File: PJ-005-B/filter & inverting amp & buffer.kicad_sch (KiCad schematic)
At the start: 27 parts, among them U11 AD8608ARUZ-REEL, U12 AD8608ARUZ-REEL

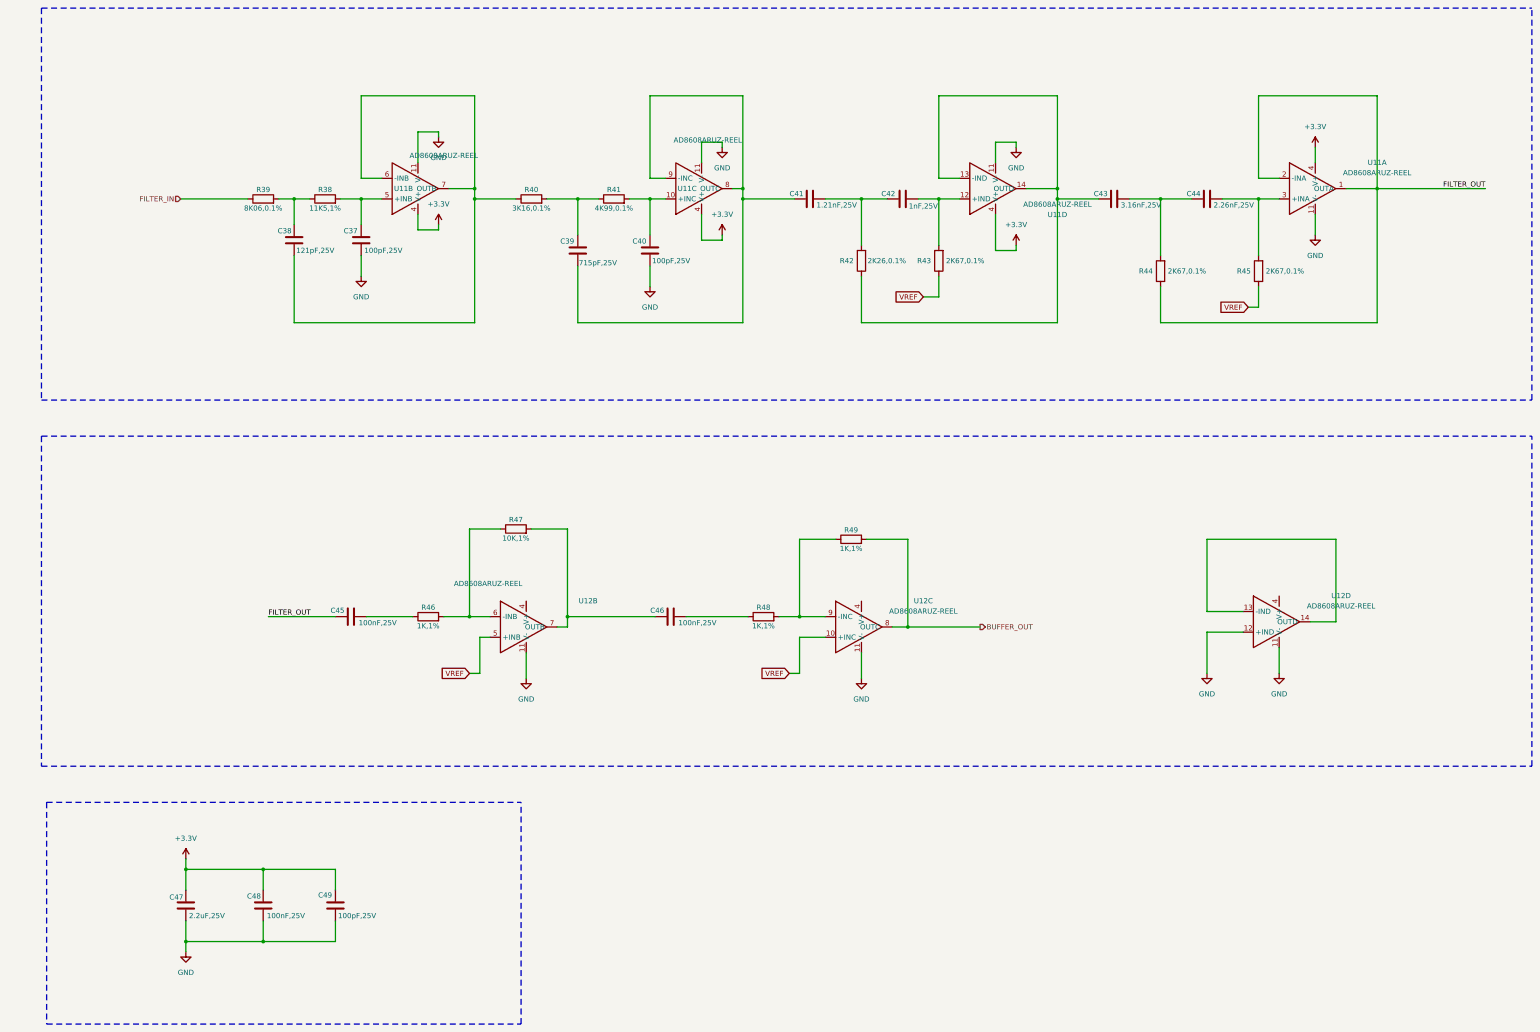
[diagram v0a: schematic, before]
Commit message: -- Receive stage with charge amp-->inverting amp-->BPF-->inverting amp-->buffer-->PGA-->buffer -- Transmit stage with push pull mosfet -- TTL to RS485 converter -- LDOs 12V to 9V, 9V to 6V, 6V to 5V, 5V to 2.5V and -5V to -2.5V
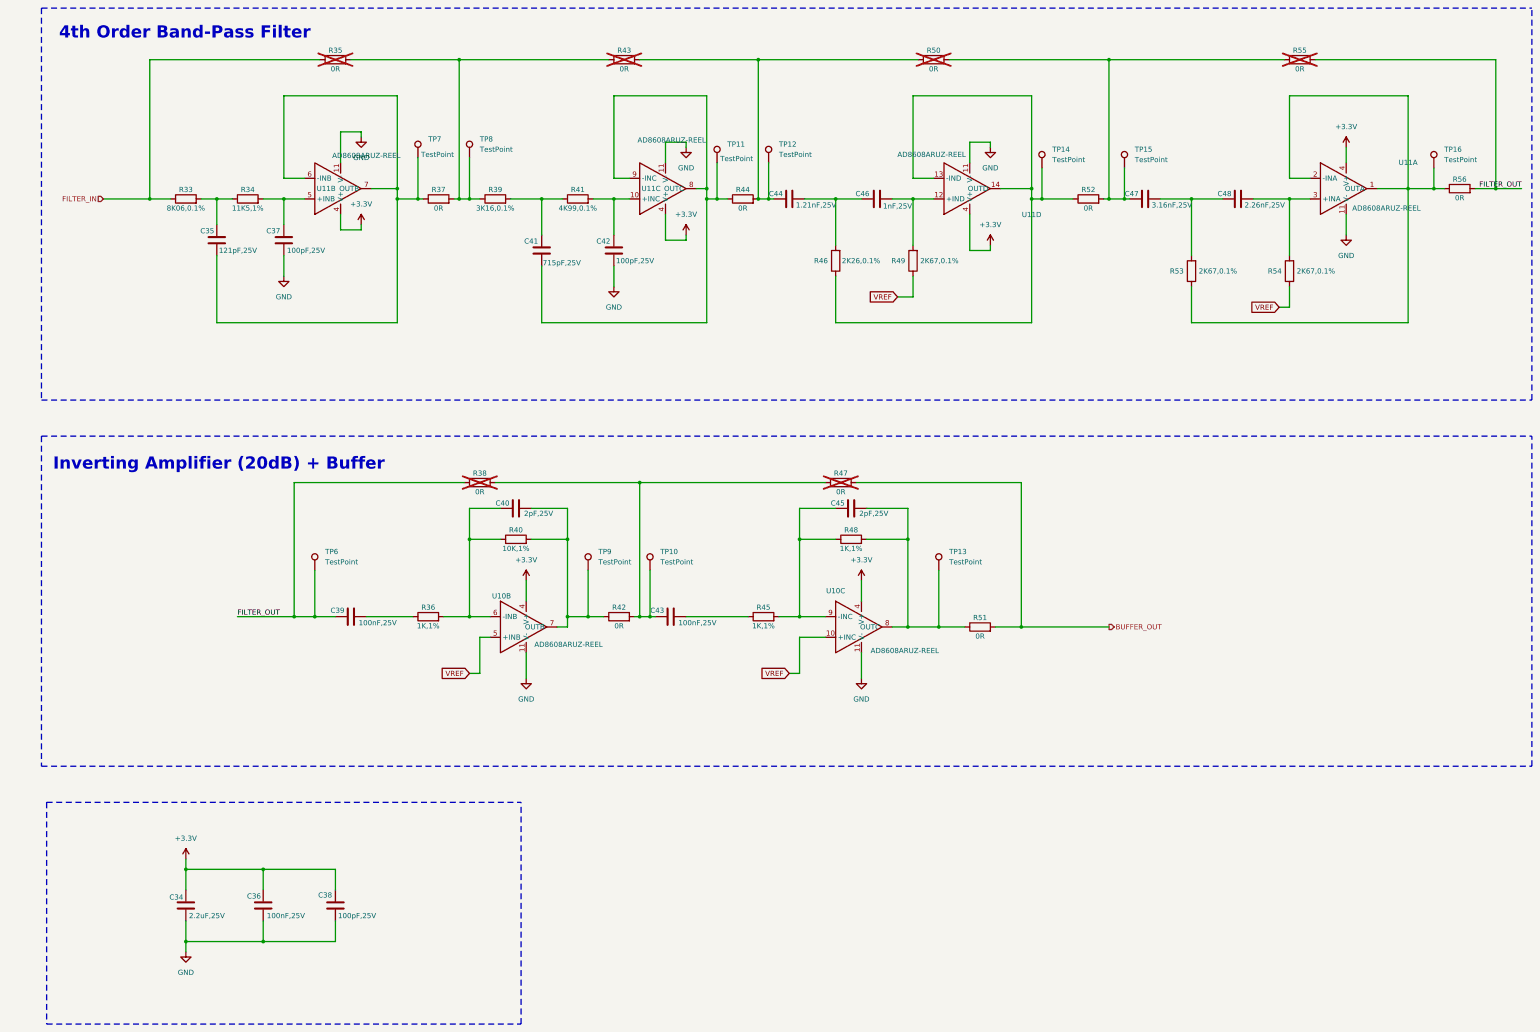
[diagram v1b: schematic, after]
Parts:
- removed unit 4 of U12
- added C40, C45: 2pF,25V, XaltenFootprints:C0603, symbol Device:C
- added R35, R37, R38, R42, R43, R44, R47, R50, R51, R52, R55, R56: 0R, XaltenFootprints:R0603, symbol Device:R
- added TP10, TP11, TP12, TP13, TP14, TP15, TP16, TP6, TP7, TP8, TP9: TestPoint, TestPoint:TestPoint_Pad_1.0x1.0mm, symbol Connector:TestPoint
- C34: renamed from C47; footprint (none) -> XaltenFootprints:C0603
- C35: renamed from C38; footprint (none) -> XaltenFootprints:C0603
- C36: renamed from C48; footprint (none) -> XaltenFootprints:C0603
- C37: footprint (none) -> XaltenFootprints:C0603
- C38: renamed from C49; footprint (none) -> XaltenFootprints:C0603
- C39: renamed from C45; footprint (none) -> XaltenFootprints:C0603
- C41: renamed from C39; footprint (none) -> XaltenFootprints:C0603
- C42: renamed from C40; footprint (none) -> XaltenFootprints:C0603
- C43: renamed from C46; footprint (none) -> XaltenFootprints:C0603
- C44: renamed from C41; footprint (none) -> XaltenFootprints:C0603
- C46: renamed from C42; footprint (none) -> XaltenFootprints:C0603
- C47: renamed from C43; footprint (none) -> XaltenFootprints:C0603
- C48: renamed from C44; footprint (none) -> XaltenFootprints:C0603
- R33: renamed from R39; footprint (none) -> XaltenFootprints:R0603
- R34: renamed from R38; footprint (none) -> XaltenFootprints:R0603
- R36: renamed from R46; footprint (none) -> XaltenFootprints:R0603
- R39: renamed from R40; footprint (none) -> XaltenFootprints:R0603
- R40: renamed from R47; footprint (none) -> XaltenFootprints:R0603
- R41: footprint (none) -> XaltenFootprints:R0603
- R45: renamed from R48; footprint (none) -> XaltenFootprints:R0603
- R46: renamed from R42; footprint (none) -> XaltenFootprints:R0603
- R48: renamed from R49; footprint (none) -> XaltenFootprints:R0603
- R49: renamed from R43; footprint (none) -> XaltenFootprints:R0603
- R53: renamed from R44; footprint (none) -> XaltenFootprints:R0603
- R54: renamed from R45; footprint (none) -> XaltenFootprints:R0603
- U10: renamed from U12; footprint (none) -> Echosounder Transceiver FP:RU_14_ADI-L
- U11: footprint (none) -> Echosounder Transceiver FP:RU_14_ADI-L
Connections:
- net +3.3V: now also U10.4 (V+), U10.4 (V+)
- net BUFFER_OUT: now also R47.2, R51.2; no longer R48.2, U10.8 (OUTC)
- net FILTER_IN: now also R35.1
- net FILTER_OUT: now also R38.1, R55.2, R56.2, TP6.1; no longer R53.1, U11.1 (OUTA), U11.2 (-INA)
- net at R46.1, U11.13 (-IND), U11.14 (OUTD): now also R52.1, TP14.1; no longer C47.1
- net at C41.2, U11.8 (OUTC), U11.9 (-INC): now also R44.1, TP11.1; no longer C44.1
- net at R36.2, R40.1, U10.6 (-INB): now also C40.1
- net at R40.2, U10.7 (OUTB): now also C40.2, R42.1, TP9.1; no longer C43.1
- net at R45.2, R48.1, U10.9 (-INC): now also C45.1
- net at C35.2, U11.6 (-INB), U11.7 (OUTB): now also R37.1, TP7.1; no longer R39.1
- new net: C44.1, R43.2, R44.2, R50.1, TP12.1
- new net: R35.2, R37.2, R39.1, R43.1, TP8.1
- new net: C47.1, R50.2, R52.2, R55.1, TP15.1
- new net: C43.1, R38.2, R42.2, R47.1, TP10.1
- new net: C45.2, R48.2, R51.1, TP13.1, U10.8 (OUTC)
- new net: R53.1, R56.1, TP16.1, U11.1 (OUTA), U11.2 (-INA)
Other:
- note added: "4th Order Band-Pass Filter"
- note added: "Inverting Amplifier (20dB) + Buffer"
- moved on the sheet: C35, C37, C41, C42, C44, C46, C47, C48, R33, R34, R39, R40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

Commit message: Transceiver After Review
-- Added bulk capacitors for -2.5V LDO
-- Added 0R for shorting RE and DE in TTL to RS485
-- Changed the snubber values in transformer primary to 2.2nF and 33R
-- Removed the 10nF and 100K in parallel with the transducer
-- Added 1000uF capacitor for transformer centre tap
-- Added 100pF decoupling capacitor for gate driver IC
--Changed secondary snubber values to 220nF and 680R
-- Changed LC inductor value to 100uH (transformer secondary)
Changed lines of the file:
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@@
 		(on_board yes)
 		(dnp no)
-		(fields_autoplaced yes)
 		(property "Reference" "#PWR078"
 			(at 102.87 82.55 0)
@@
 		)
 		(property "Value" "+3.3V"
-			(at 102.87 73.66 0)
+			(at 105.918 79.502 0)
 			(effects
 				(font
@@
 		(dnp no)
 		(property "Reference" "U11"
-			(at 174.244 69.85 0)
+			(at 171.196 62.23 0)
 			(effects
 				(font
@@
 		)
 		(property "Value" "AD8608ARUZ-REEL"
-			(at 179.324 57.912 0)
+			(at 186.436 75.946 0)
 			(effects
 				(font
@@
 		(on_board yes)
 		(dnp no)
-		(fields_autoplaced yes)
 		(property "Reference" "#PWR082"
 			(at 182.88 66.04 0)
@@
 		)
 		(property "Value" "GND"
-			(at 182.88 64.77 0)
+			(at 182.88 63.5 0)
 			(effects
 				(font
@@
 		(dnp no)
 		(property "Reference" "U11"
-			(at 360.68 63.4298 0)
+			(at 339.09 62.484 0)
 			(effects
 				(font
@@
 		(dnp no)
 		(property "Reference" "U11"
-			(at 94.234 69.85 0)
+			(at 90.424 61.976 0)
 			(effects
 				(font
@@
 		)
 		(property "Value" "AD8608ARUZ-REEL"
-			(at 104.14 61.722 0)
+			(at 107.188 74.168 0)
 			(effects
 				(font
@@
 		(on_board yes)
 		(dnp no)
-		(fields_autoplaced yes)
 		(property "Reference" "#PWR083"
 			(at 182.88 85.09 0)
@@
 		)
 		(property "Value" "+3.3V"
-			(at 182.88 76.2 0)
+			(at 182.88 83.82 0)
 			(effects
 				(font
@@
 		(dnp no)
 		(property "Reference" "U11"
-			(at 267.97 76.2702 0)
+			(at 246.634 62.23 0)
 			(effects
 				(font
@@
 		)
 		(property "Value" "AD8608ARUZ-REEL"
-			(at 243.332 61.468 0)
+			(at 262.382 73.66 0)
 			(effects
 				(font
